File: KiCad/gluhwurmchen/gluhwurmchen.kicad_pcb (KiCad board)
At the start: 2 copper layers, 30.6 x 30.6 mm, 13 parts, among them J1 3V_ext, J2 GND_ext, Q1 2N3904, U1 CR2032

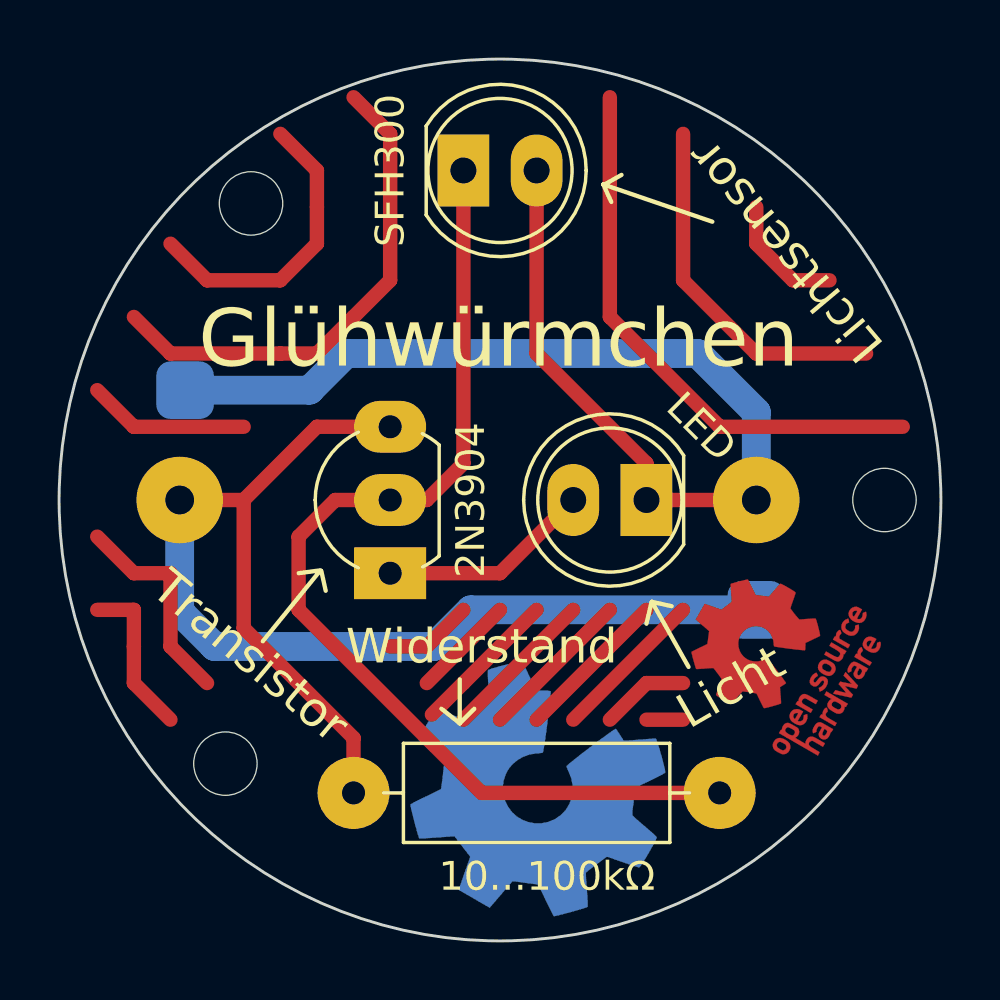
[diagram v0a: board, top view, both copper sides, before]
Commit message: english translation
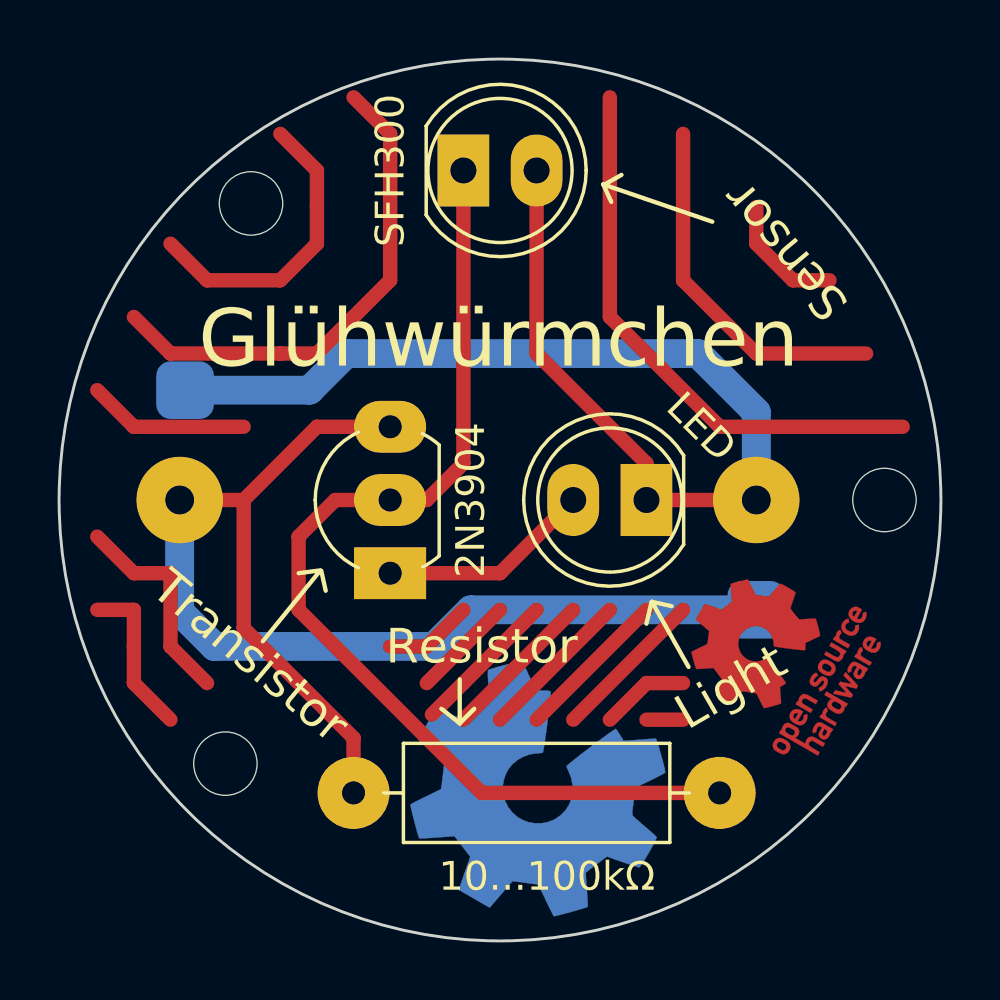
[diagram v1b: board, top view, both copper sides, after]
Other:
- board text added: "Light"
- board text added: "Resistor"
- board text added: "Sensor"
- board text removed: "Licht"
- board text removed: "Lichtsensor"
- board text removed: "Widerstand"
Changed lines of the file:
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@@
     (effects (font (size 1.2 1.2) (thickness 0.2)))
   )
-  (gr_text "Widerstand" (at 81.915 93.98) (layer "F.SilkS")
+  (gr_text "Resistor" (at 81.915 93.98) (layer "F.SilkS")
     (effects (font (size 1.2 1.2) (thickness 0.2)))
   )
-  (gr_text "Lichtsensor" (at 92.456 80.264 -230) (layer "F.SilkS")
+  (gr_text "Sensor" (at 92.456 80.264 -230) (layer "F.SilkS")
     (effects (font (size 1.2 1.2) (thickness 0.2)))
   )
@@
     (effects (font (size 2 2) (thickness 0.3)))
   )
-  (gr_text "Licht" (at 90.551 95.377 30) (layer "F.SilkS")
+  (gr_text "Light" (at 90.551 95.377 30) (layer "F.SilkS")
     (effects (font (size 1.2 1.2) (thickness 0.2)))
   )
